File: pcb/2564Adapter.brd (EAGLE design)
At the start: 35.6 x 21.6 mm, 7 parts, among them IC1 TMS2564, IC2 EPROM, IC4 74LS00N

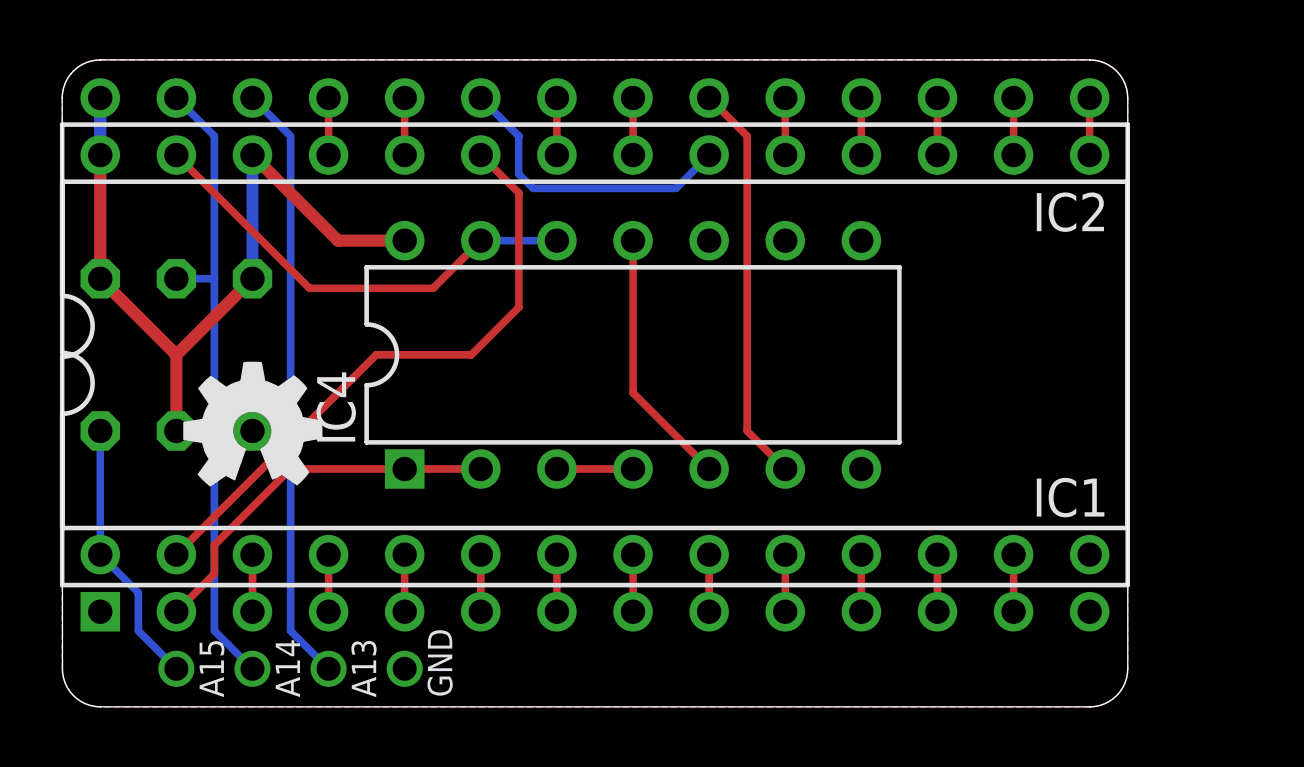
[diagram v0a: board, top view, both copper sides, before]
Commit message: PCB Updates and BOM cleanup
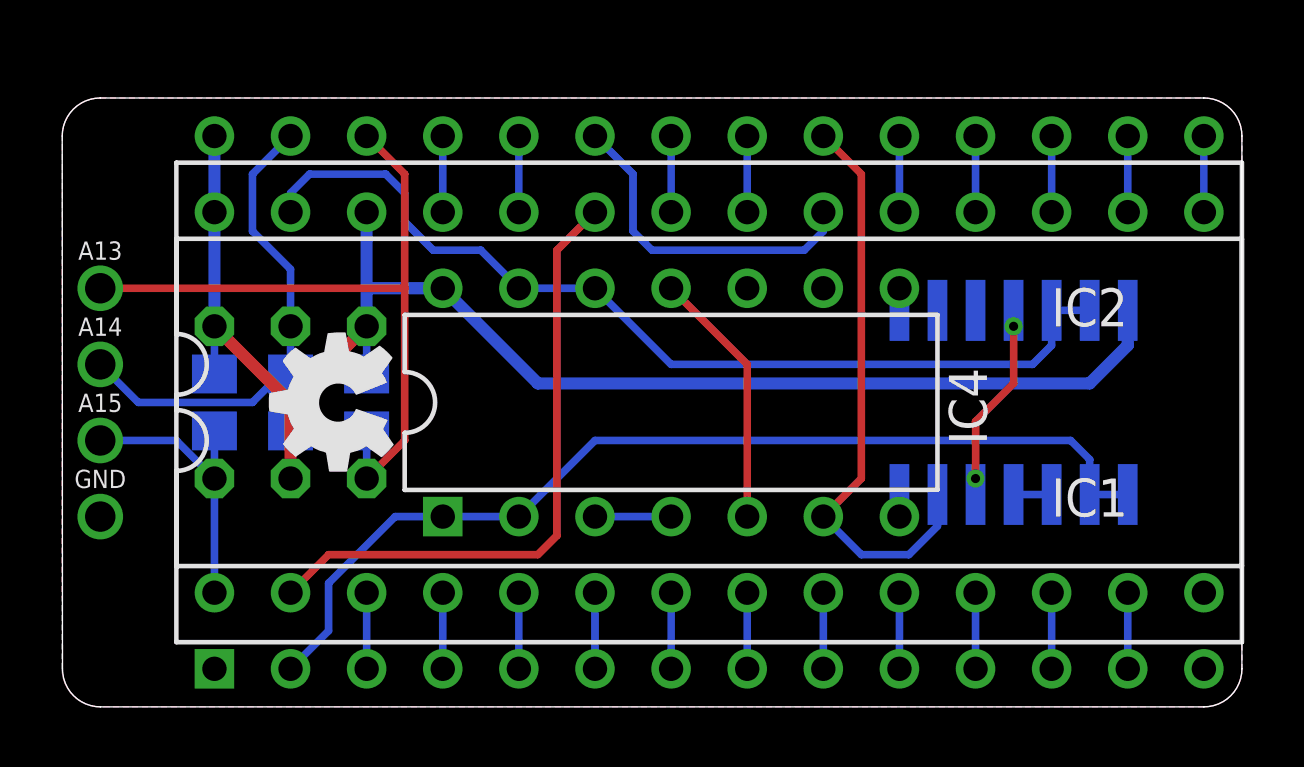
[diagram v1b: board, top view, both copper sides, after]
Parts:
- added IC3: 74S00D, 74xx-us:SO14
- added R4, R5, R6: 10K, resistor:R0805
- added X1: (no value), con-lstb-rp:MA04-1
- moved IC1 4.26 mm to (21.6, 8.89)
- moved R1 4.13 mm to (10.2, 10.2)
- moved R2 4.13 mm to (7.62, 10.2)
- moved R3 4.13 mm to (5.08, 10.2)
- moved IC2 4.02 mm to (21.6, 11.4)
- moved GOLD_ORB_SM1 3.01 mm to (9.21, 10.2), turned to 90 degrees
- moved IC4 2.03 mm to (20.3, 10.2)
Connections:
- new net N$3: IC3.3, IC3.4
- new net N$4: IC3.11, IC3.5
- net !CE: now also IC3.6
- net !CS1: now also IC3.1, IC3.2
- net !CS2: now also IC3.12, IC3.13
- net A13: now also R4.1, X1.4
- net A14: now also R5.1, X1.3
- net A15: now also R6.1, X1.2
- net GND: now also IC3.10, IC3.7, IC3.9, X1.1
- net VCC: now also IC3.14, R4.2, R5.2, R6.2
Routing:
- net VCC: track 26.1 -> 53.1 mm
- net !CS1: track 12.7 -> 33.5 mm
- net !CS2: track 15.2 -> 32.2 mm
- net N$4: track 0.00 -> 6.67 mm, vias 0 -> 2
- net !CE: track 13.4 -> 19.5 mm
- net A14: track 21.4 -> 16.3 mm, vias 1 -> 0
- net A13: track 21.4 -> 24.2 mm, vias 1 -> 0
- net N$3: track 0.00 -> 1.27 mm
- net A11: track 10.1 -> 11.2 mm
- net A15: track 8.99 -> 9.74 mm, vias 1 -> 0
- net D2: track 1.91 -> 2.54 mm
- net D1: track 1.91 -> 2.54 mm
- net D0: track 1.91 -> 2.54 mm
- net A7: track 1.91 -> 2.54 mm
- net A6: track 1.91 -> 2.54 mm
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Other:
- board size 35.6 x 21.6 mm -> 39.4 x 20.3 mm
